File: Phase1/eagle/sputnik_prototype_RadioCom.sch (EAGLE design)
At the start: 73 parts, among them Y1 32MHz

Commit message: added notes
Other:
- note added: "TODO: -Fix RF GND -2mm 2x22pin custom part and placement (83B-44PA-2DS(71)-ND) (H123075-ND) -EN line on PA to KW0x"
- note removed: "TODO: -Fix RF GND"
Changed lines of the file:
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@@
 <?xml version="1.0" encoding="utf-8"?>
 <!DOCTYPE eagle SYSTEM "eagle.dtd">
-<eagle version="7.5.0">
+<eagle version="7.4.0">
 <drawing>
 <settings>
@@
 <wire x1="60.96" y1="149.86" x2="7.62" y2="149.86" width="0.1524" layer="97" style="longdash"/>
 <wire x1="7.62" y1="149.86" x2="7.62" y2="200.66" width="0.1524" layer="97" style="longdash"/>
-<text x="99.06" y="116.84" size="1.778" layer="97">TODO:
--Fix RF GND</text>
+<text x="86.36" y="116.84" size="1.778" layer="97">TODO:
+-Fix RF GND
+-2mm 2x22pin custom part and placement (83B-44PA-2DS(71)-ND)
+(H123075-ND)
+-EN line on PA to KW0x</text>
 </plain>
 <instances>

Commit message: Added 22 pinout, no footprint yet, also did RF_GND
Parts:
- added X2: 332-22, con-garry:332-22
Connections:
- new net N$32: KW0X.PTE3, X2-2.S
- new net N$33: KW0X.PTE16, X2-3.S
- new net N$35: KW0X.PTE17, X2-4.S
- new net N$36: KW0X.PTE18, X2-5.S
- new net N$37: KW0X.PTE19, X2-6.S
- new net N$38: KW0X.PTE30, X2-7.S
- new net N$4: KW0X.PTE2, X2-1.S
- new net PA_EN: KW0X.PTE1, U$9.EN
- new net PTB0: KW0X.PTB0
- new net PTB1: KW0X.PTB1, X2-12.S
- new net PTB17: KW0X.PTB17, X2-14.S
- new net PTB2: KW0X.PTB2, X2-13.S
- new net PTBO: X2-11.S
- new net PTC1: KW0X.PTC1, X2-15.S
- new net PTC2: KW0X.PTC2, X2-16.S
- new net PTC3: KW0X.PTC3, X2-17.S
- new net PTC4: KW0X.PTC4, X2-18.S
- new net PTC5: KW0X.PTC5, X2-19.S
- new net PTC6: KW0X.PTC6, X2-20.S
- new net RF_RESET: X2-21.S
- new net SOMETHING: KW0X.RESET(RF)
- net GND: now also U$9.PG
- net PE0/UART0RX: now also X2-8.S
- net PE1/UART0TX: now also X2-9.S
- net PE3: now also X2-10.S
- net V+: now also X2-22.S; no longer U$9.EN
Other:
- note added: "All these go to 22 pinout"
- note added: "RF/DC GND connection"
- note added: "TODO: -Make footprint for 22pin (83B-44PA-2DS(71)-ND) (H123075-ND) -Switch"
- note removed: "TODO: -Fix RF GND -2mm 2x22pin custom part and placement (83B-44PA-2DS(71)-ND) (H123075-ND) -EN line on PA to KW0x"
- moved on the sheet: C28, C29, TP6, TP7

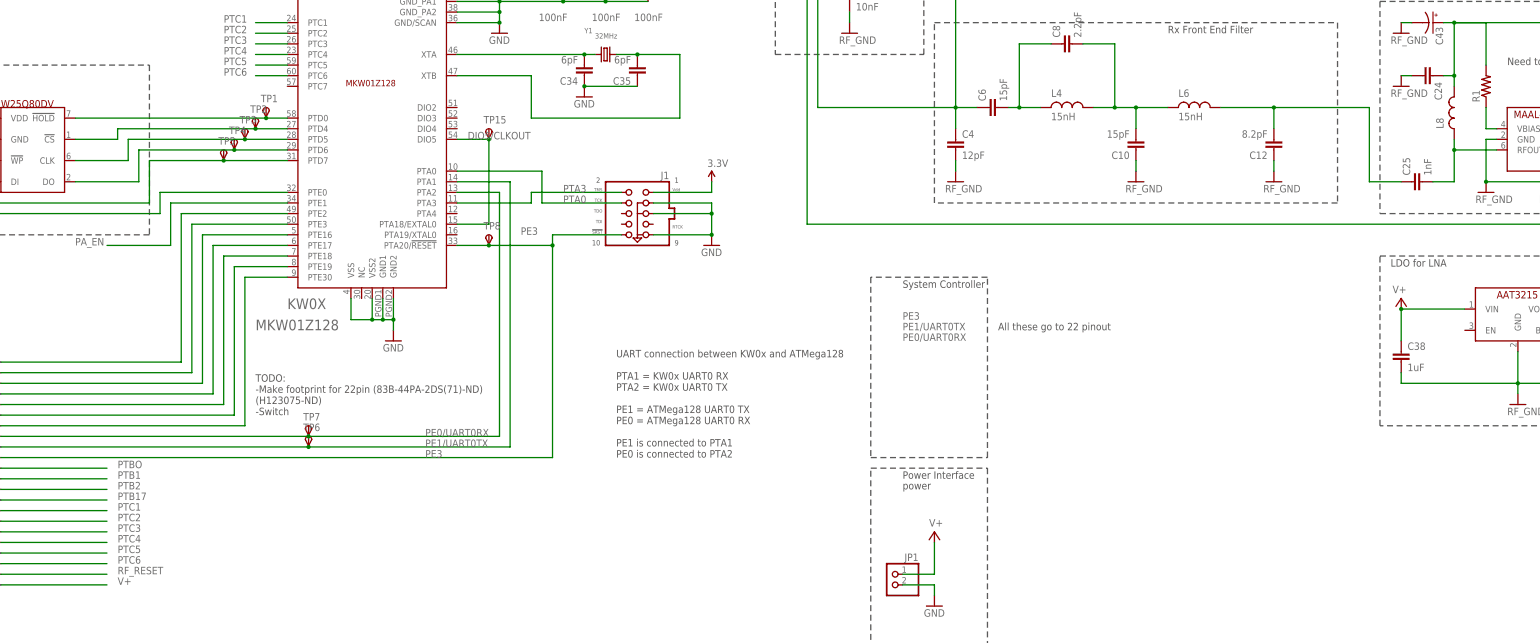
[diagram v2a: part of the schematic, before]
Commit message: Updated Enable lines, switch is gonna be moved to SysCon board
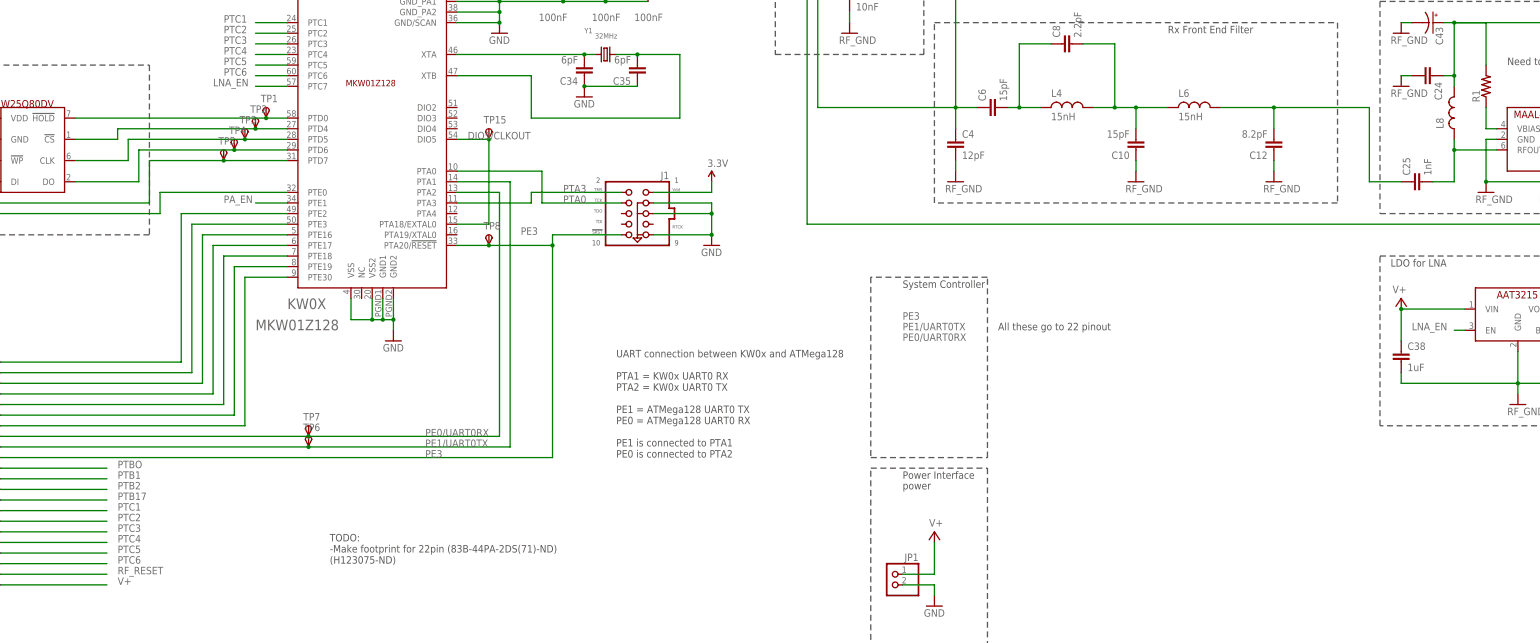
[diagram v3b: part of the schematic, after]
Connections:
- new net LNA_EN: KW0X.PTC7, U$7.EN
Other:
- note added: "TODO: -Make footprint for 22pin (83B-44PA-2DS(71)-ND) (H123075-ND)"
- note removed: "TODO: -Make footprint for 22pin (83B-44PA-2DS(71)-ND) (H123075-ND) -Switch"
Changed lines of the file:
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@@
 <wire x1="60.96" y1="160.02" x2="7.62" y2="160.02" width="0.1524" layer="97" style="longdash"/>
 <wire x1="7.62" y1="160.02" x2="7.62" y2="200.66" width="0.1524" layer="97" style="longdash"/>
-<text x="86.36" y="116.84" size="1.778" layer="97">TODO:
+<text x="104.14" y="81.28" size="1.778" layer="97">TODO:
 -Make footprint for 22pin (83B-44PA-2DS(71)-ND)
-(H123075-ND)
--Switch</text>
+(H123075-ND)</text>
 <text x="264.16" y="137.16" size="1.778" layer="97">All these go to 22 pinout</text>
 <wire x1="353.06" y1="233.68" x2="248.92" y2="233.68" width="0.1524" layer="97" style="longdash"/>
@@
 <segment>
 <pinref part="KW0X" gate="G$1" pin="PTE1"/>
-<wire x1="93.98" y1="167.64" x2="66.04" y2="167.64" width="0.1524" layer="91"/>
-<wire x1="66.04" y1="167.64" x2="66.04" y2="157.48" width="0.1524" layer="91"/>
-<wire x1="66.04" y1="157.48" x2="50.8" y2="157.48" width="0.1524" layer="91"/>
-<label x="43.18" y="157.48" size="1.778" layer="95"/>
+<wire x1="93.98" y1="167.64" x2="86.36" y2="167.64" width="0.1524" layer="91"/>
+<label x="78.74" y="167.64" size="1.778" layer="95"/>
 </segment>
 </net>
@@
 </segment>
 </net>
+<net name="LNA_EN" class="0">
+<segment>
+<pinref part="KW0X" gate="G$1" pin="PTC7"/>
+<wire x1="93.98" y1="195.58" x2="86.36" y2="195.58" width="0.1524" layer="91"/>
+<label x="76.2" y="195.58" size="1.778" layer="95"/>
+</segment>
+<segment>
+<pinref part="U$7" gate="G$1" pin="EN"/>
+<wire x1="375.92" y1="137.16" x2="373.38" y2="137.16" width="0.1524" layer="91"/>
+<label x="363.22" y="137.16" size="1.778" layer="95"/>
+</segment>
+</net>

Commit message: fixed symbols
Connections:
- net N$20 renamed LNA_OUT
- net N$5 renamed LNA_IN
- removed net N$2 (its old number): C24.1, C43.+, L8.2, R1.2
- removed net N$9: C36.1, U$7.VOUT
- new net VBIAS: C24.1, C36.1, C43.+, L8.2, R1.2, U$7.VOUT
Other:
- note added: "Rx Low Noise Amplifier & LDO"
- note added: "Tx Power Amplifier & LDO"
- note removed: "LDO for LNA"
- note removed: "LDO for Power Amplifier"
- note removed: "Rx Low Noise Amplifier"
- note removed: "Tx Power Amplifier"
- moved on the sheet: C15, C16, C18, C19, C20, C21, C22, C23, C24, C25, C43, L7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

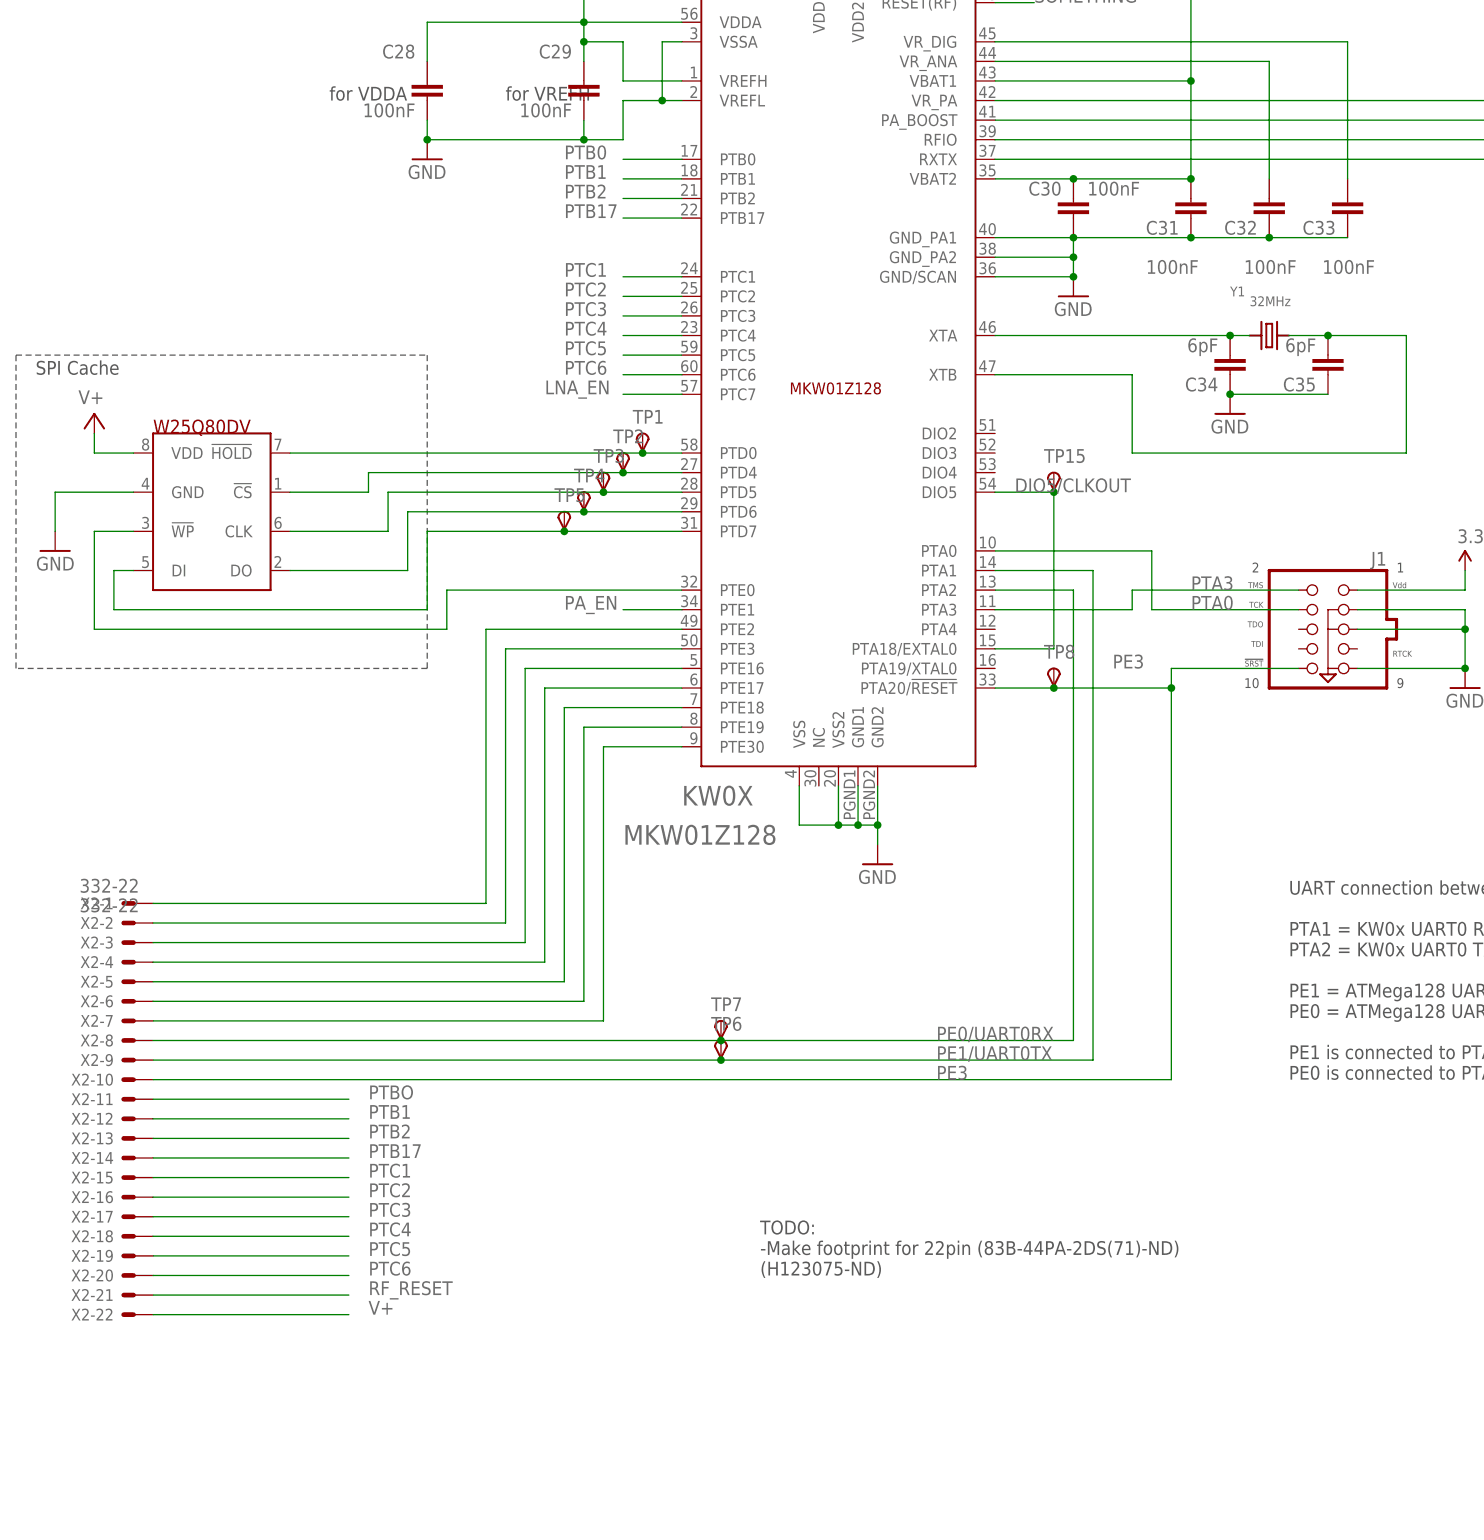
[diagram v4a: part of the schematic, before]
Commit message: Added GPIO bus
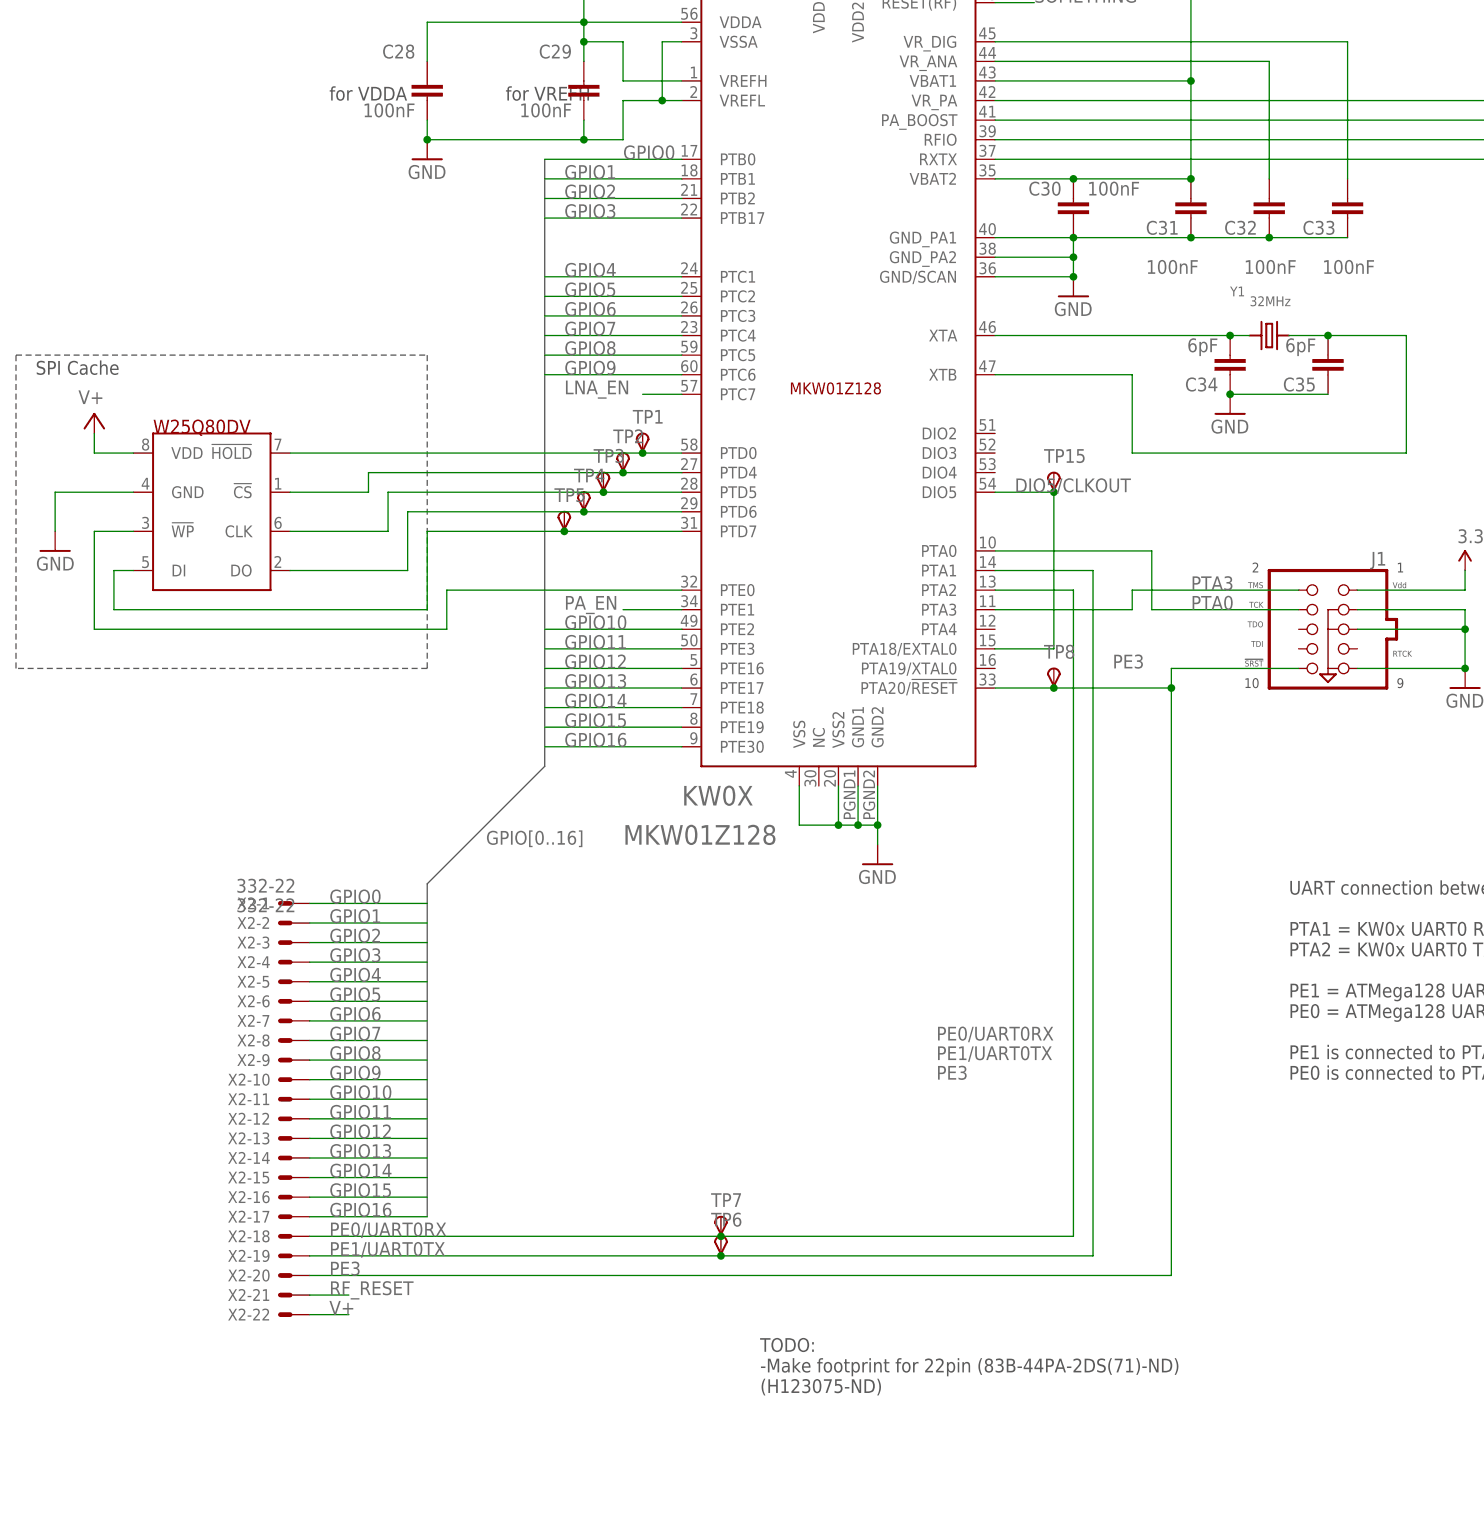
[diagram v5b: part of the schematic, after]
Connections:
- removed net N$32: KW0X.PTE3, X2-2.S
- removed net N$33: KW0X.PTE16, X2-3.S
- removed net N$35: KW0X.PTE17, X2-4.S
- removed net N$36: KW0X.PTE18, X2-5.S
- removed net N$37: KW0X.PTE19, X2-6.S
- removed net N$38: KW0X.PTE30, X2-7.S
- removed net N$4: KW0X.PTE2, X2-1.S
- removed net PTB0: KW0X.PTB0
- removed net PTB1: KW0X.PTB1, X2-12.S
- removed net PTB17: KW0X.PTB17, X2-14.S
- removed net PTB2: KW0X.PTB2, X2-13.S
- removed net PTBO: X2-11.S
- removed net PTC1: KW0X.PTC1, X2-15.S
- removed net PTC2: KW0X.PTC2, X2-16.S
- removed net PTC3: KW0X.PTC3, X2-17.S
- removed net PTC4: KW0X.PTC4, X2-18.S
- removed net PTC5: KW0X.PTC5, X2-19.S
- removed net PTC6: KW0X.PTC6, X2-20.S
- new net GPIO0: KW0X.PTB0, X2-1.S
- new net GPIO1: KW0X.PTB1, X2-2.S
- new net GPIO10: KW0X.PTE2, X2-11.S
- new net GPIO11: KW0X.PTE3, X2-12.S
- new net GPIO12: KW0X.PTE16, X2-13.S
- new net GPIO13: KW0X.PTE17, X2-14.S
- new net GPIO14: KW0X.PTE18, X2-15.S
- new net GPIO15: KW0X.PTE19, X2-16.S
- new net GPIO16: KW0X.PTE30, X2-17.S
- new net GPIO2: KW0X.PTB2, X2-3.S
- new net GPIO3: KW0X.PTB17, X2-4.S
- new net GPIO4: KW0X.PTC1, X2-5.S
- new net GPIO5: KW0X.PTC2, X2-6.S
- new net GPIO6: KW0X.PTC3, X2-7.S
- new net GPIO7: KW0X.PTC4, X2-8.S
- new net GPIO8: KW0X.PTC5, X2-9.S
- new net GPIO9: KW0X.PTC6, X2-10.S
- net PE0/UART0RX: now also X2-18.S; no longer X2-8.S
- net PE1/UART0TX: now also X2-19.S; no longer X2-9.S
- net PE3: now also X2-20.S; no longer X2-10.S
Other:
- moved on the sheet: TP6, TP7, X2-1, X2-10, X2-11, X2-12, X2-13, X2-14, X2-15, X2-16, X2-17, X2-18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
